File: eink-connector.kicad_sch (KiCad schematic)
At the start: 6 parts, among them J2 FFC-FPC_1X24_PIN

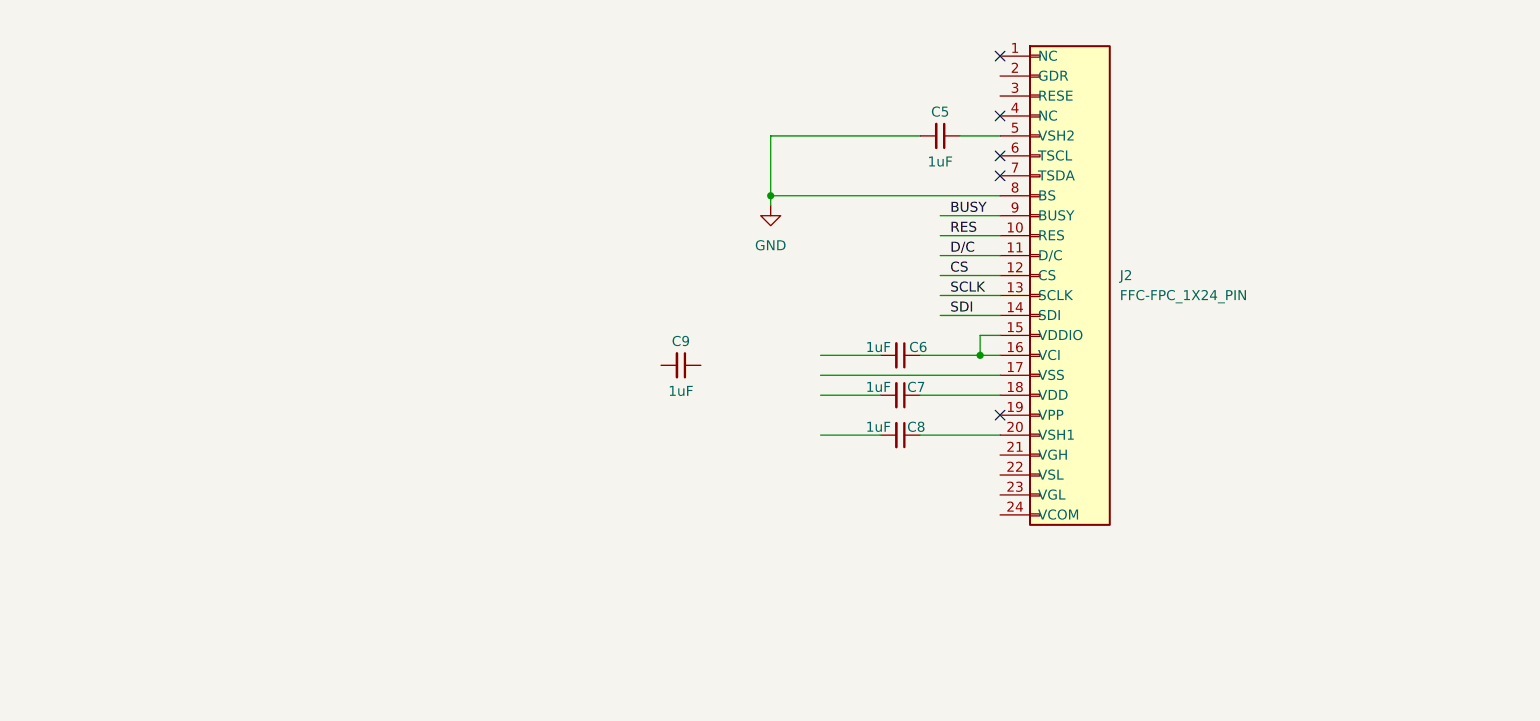
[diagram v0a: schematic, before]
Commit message: eink-> mcu connections
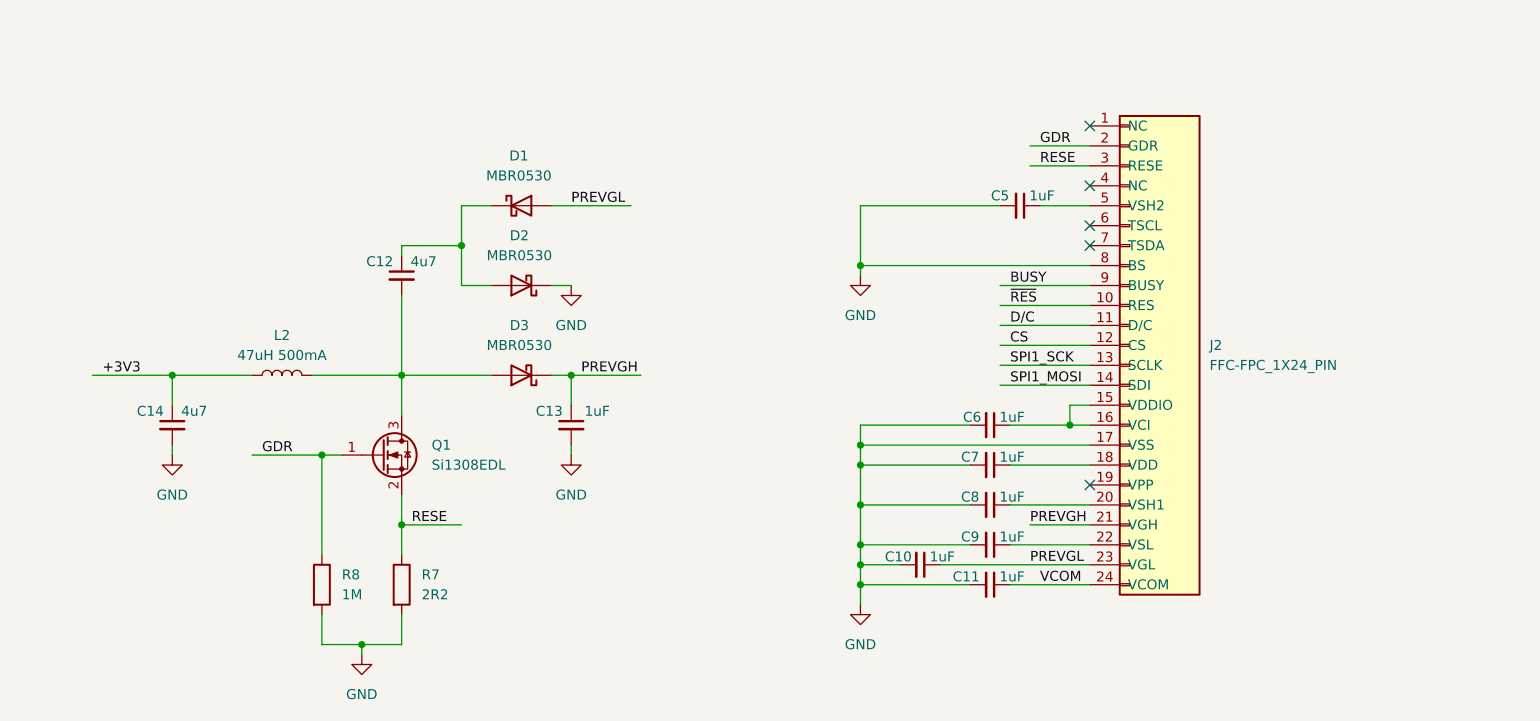
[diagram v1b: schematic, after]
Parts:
- added C10, C11, C13: 1uF, Capacitor_SMD:C_0603_1608Metric, symbol Device:C_Small
- added C12, C14: 4u7, Capacitor_SMD:C_0603_1608Metric, symbol Device:C_Small
- added D1, D2, D3: MBR0530, Diode_SMD:D_SOD-123, symbol Diode:MBR0530
- added L2: 47uH 500mA, 47uH 500mA, symbol Device:L
- added Q1: Si1308EDL, Package_TO_SOT_SMD:SOT-323_SC-70, symbol Transistor_FET:Si1308EDL
- added R7: 2R2, Resistor_SMD:R_0201_0603Metric, symbol Device:R
- added R8: 1M, Resistor_SMD:R_0201_0603Metric, symbol Device:R
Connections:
- net GND: now also C6.2, C7.2, C8.2, C9.2, J2.17 (VSS), C10.2, C11.2, C13.2, C14.2, D2.1 (K), R7.2, R8.2
- net GDR: now reaches J2.2 (GDR)
- net GDR: now also Q1.1 (G), R8.1
- net PREVGH: now reaches J2.21 (VGH)
- net PREVGH: now also C13.1, D3.1 (K)
- net at J2.22 (VSL): now also C9.1
- net PREVGL: now reaches J2.23 (VGL)
- net PREVGL: now also C10.1, D1.2 (A)
- net VCOM: now reaches J2.24 (VCOM)
- net VCOM: now also C11.1
- net RESE: now reaches J2.3 (RESE)
- net RESE: now also Q1.2 (S), R7.1
- net RES renamed ~{RES}
- net SCLK renamed SPI1_SCK
- net SDI renamed SPI1_MOSI
- new net: C12.2, D3.2 (A), L2.2, Q1.3 (D)
- new net: C12.1, D1.1 (K), D2.2 (A)
- new net +3V3: C14.1, L2.1
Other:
- moved on the sheet: C5, C6, C7, J2

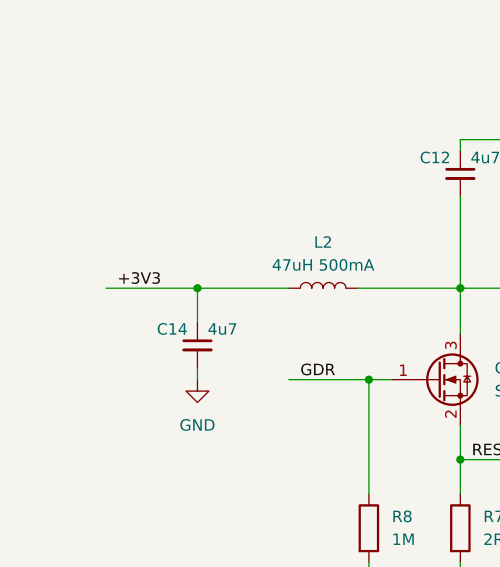
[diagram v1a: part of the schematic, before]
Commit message: added externals crystal oscillators
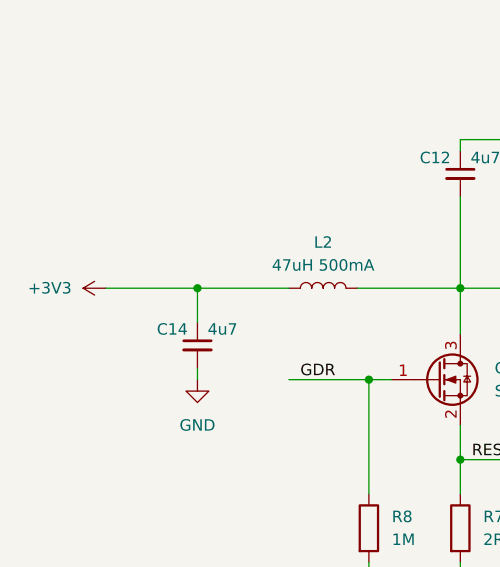
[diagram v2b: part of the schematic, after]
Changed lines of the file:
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@@
-		)
-	)
-	(label "+3V3"
-		(at 72.39 95.25 0)
-		(effects
-			(font
-				(size 1.27 1.27)
-			)
-			(justify left bottom)
 		)
 	)
@@
 					(unit 1)
 				)
+			)
+		)
+	)
+	(symbol
+		(lib_id "power:+3V3")
+		(at 71.12 95.25 90)
+		(unit 1)
+		(exclude_from_sim no)
+		(in_bom yes)
+		(on_board yes)
+		(dnp no)
+		(fields_autoplaced yes)
+		(property "Reference" "#PWR025"
+			(at 74.93 95.25 0)
+			(effects
+				(font
+					(size 1.27 1.27)
+				)
+				(hide yes)
+			)
+		)
+		(property "Value" "+3V3"
+			(at 67.31 95.2499 90)
+			(effects
+				(font
+					(size 1.27 1.27)
+				)
+				(justify left)
+			)
+		)
+		(property "Footprint" ""
+			(at 71.12 95.25 0)
+			(effects
+				(font
+					(size 1.27 1.27)
+				)
+				(hide yes)
+			)
+		)
+		(property "Datasheet" ""
+			(at 71.12 95.25 0)
+			(effects
+				(font
+					(size 1.27 1.27)
+				)
+				(hide yes)
+			)
+		)
+		(property "Description" "Power symbol creates a global label with name \"+3V3\""
+			(at 71.12 95.25 0)
+			(effects
+				(font
+					(size 1.27 1.27)
+				)
+				(hide yes)
+			)
+		)
+		(pin "1"
+		)
+		(instances
+			(project ""
+				(path "/29eb74dc-e91c-4cc5-ad9f-7f8caf36d690/d1e239c8-1e89-4f3e-9b45-1354c48c8e66"
+					(reference "#PWR025")
+					(unit 1)
+				)

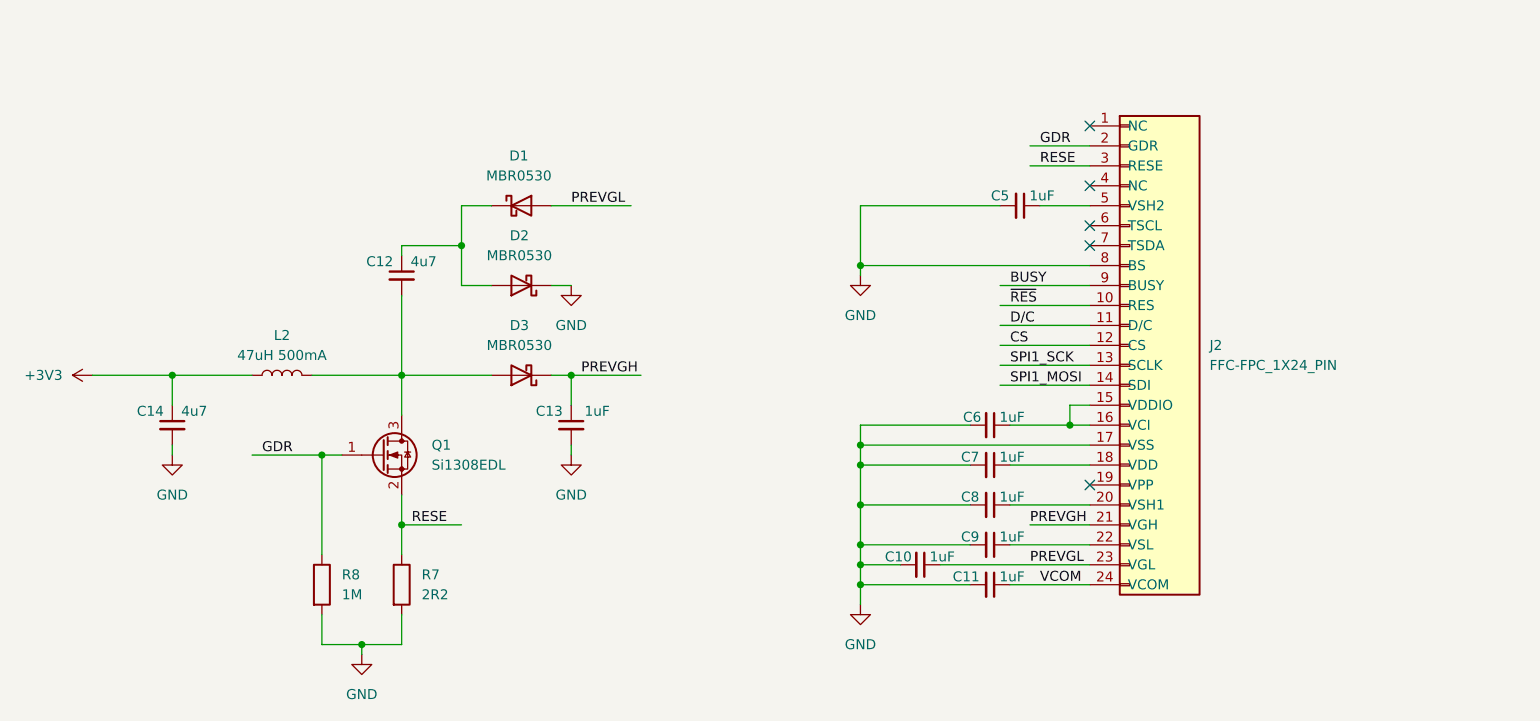
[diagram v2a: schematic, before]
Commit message: cleaned up some net labels for ERC
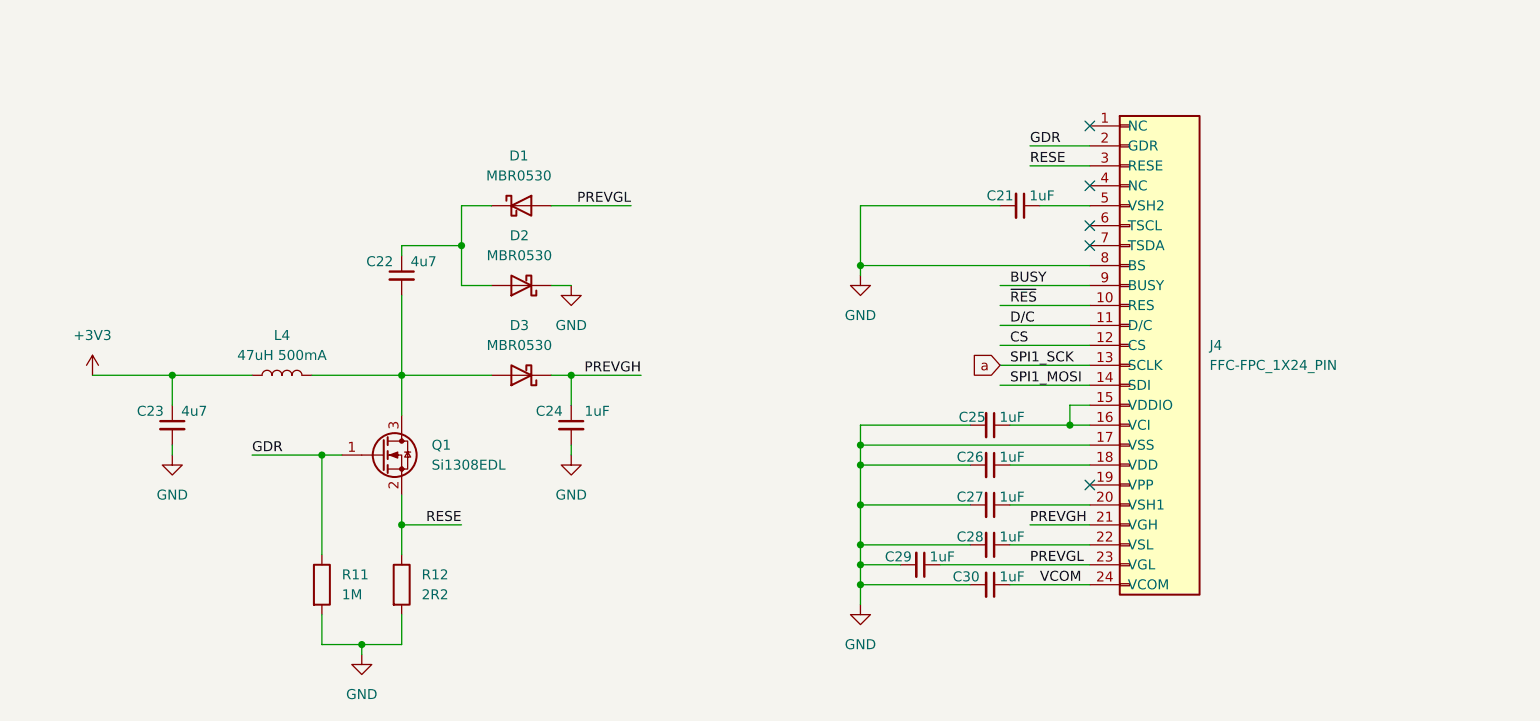
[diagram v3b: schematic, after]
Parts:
- L4: renamed from L2; footprint 47uH 500mA -> (none)
- renumbered C5 to C21, C12 to C22, C14 to C23, C13 to C24, C6 to C25, C7 to C26, C8 to C27, C9 to C28, C10 to C29, C11 to C30, J2 to J4, R8 to R11, R7 to R12
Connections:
- net SPI1_SCK renamed a
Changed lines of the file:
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@@
 	(wire
 		(pts
-			(xy 139.7 73.66) (xy 129.54 73.66)
+			(xy 129.54 73.66) (xy 139.7 73.66)
 		)
 		(stroke
@@
 	(wire
 		(pts
+			(xy 91.44 105.41) (xy 100.33 105.41)
+		)
+		(stroke
+			(width 0)
+			(type default)
+		)
+	)
+	(wire
+		(pts
 			(xy 118.11 73.66) (xy 121.92 73.66)
 		)
@@
 		(pts
 			(xy 168.91 73.66) (xy 186.69 73.66)
-		)
-		(stroke
-			(width 0)
-			(type default)
-		)
-	)
-	(wire
-		(pts
-			(xy 91.44 105.41) (xy 100.33 105.41)
 		)
 		(stroke
@@
 	)
 	(label "RESE"
-		(at 191.77 68.58 0)
+		(at 190.5 68.58 0)
 		(effects
 			(font
@@
 	)
 	(label "PREVGL"
-		(at 132.08 73.66 0)
+		(at 139.7 73.66 180)
 		(effects
 			(font
 				(size 1.27 1.27)
 			)
-			(justify left bottom)
+			(justify right bottom)
 		)
 	)
@@
 	)
 	(label "PREVGH"
-		(at 133.35 95.25 0)
+		(at 140.97 95.25 180)
 		(effects
 			(font
 				(size 1.27 1.27)
 			)
-			(justify left bottom)
+			(justify right bottom)
 		)
 	)
@@
 	)
 	(label "GDR"
-		(at 191.77 66.04 0)
+		(at 190.5 66.04 0)
 		(effects
 			(font
@@
 	)
 	(label "RESE"
-		(at 111.76 114.3 0)
+		(at 118.11 114.3 180)
 		(effects
 			(font
 				(size 1.27 1.27)
 			)
-			(justify left bottom)
+			(justify right bottom)
 		)
 	)
@@
 	)
 	(label "GDR"
-		(at 92.71 105.41 0)
+		(at 91.44 105.41 0)
 		(effects
 			(font
@@
 		)
 	)
+	(global_label "a"
+		(shape input)
+		(at 186.69 93.98 180)
+		(fields_autoplaced yes)
+		(effects
+			(font
+				(size 1.27 1.27)
+			)
+			(justify right)
+		)
+		(property "Intersheetrefs" "${INTERSHEET_REFS}"
+			(at 182.5558 93.98 0)
+			(effects
+				(font
+					(size 1.27 1.27)
+				)
+				(justify right)
+				(hide yes)
+			)
+		)
+	)
 	(symbol
 		(lib_id "Diode:MBR0530")
@@
 		(on_board yes)
 		(dnp no)
-		(property "Reference" "#PWR013"
+		(property "Reference" "#PWR039"
 			(at 168.91 130.81 0)
 			(effects
@@
 			(project "2tonewatch"
 				(path "/29eb74dc-e91c-4cc5-ad9f-7f8caf36d690/d1e239c8-1e89-4f3e-9b45-1354c48c8e66"
-					(reference "#PWR013")
+					(reference "#PWR039")
 					(unit 1)
 				)
@@
 		(on_board yes)
 		(dnp no)
-		(property "Reference" "C12"
+		(property "Reference" "C22"
 			(at 107.696 80.772 0)
 			(effects
@@
 			(project "2tonewatch"
 				(path "/29eb74dc-e91c-4cc5-ad9f-7f8caf36d690/d1e239c8-1e89-4f3e-9b45-1354c48c8e66"
-					(reference "C12")
+					(reference "C22")
 					(unit 1)
 				)
@@
 	(symbol
 		(lib_id "power:+3V3")
-		(at 71.12 95.25 90)
+		(at 71.12 95.25 0)
 		(unit 1)
 		(exclude_from_sim no)
@@
 		(dnp no)
 		(fields_autoplaced yes)
-		(property "Reference" "#PWR025"
-			(at 74.93 95.25 0)
+		(property "Reference" "#PWR036"
+			(at 71.12 99.06 0)
 			(effects
 				(font
@@
 		)
 		(property "Value" "+3V3"
-			(at 67.31 95.2499 90)
-			(effects
-				(font
-					(size 1.27 1.27)
-				)
-				(justify left)
+			(at 71.12 90.17 0)
+			(effects
+				(font
+					(size 1.27 1.27)
+				)
 			)
 		)
@@
 			(project ""
 				(path "/29eb74dc-e91c-4cc5-ad9f-7f8caf36d690/d1e239c8-1e89-4f3e-9b45-1354c48c8e66"
-					(reference "#PWR025")
+					(reference "#PWR036")
 					(unit 1)
 				)
@@
 		(on_board yes)
 		(dnp no)
-		(property "Reference" "C11"
+		(property "Reference" "C30"
 			(at 182.372 120.904 90)
 			(effects
@@
 			(project "2tonewatch"
 				(path "/29eb74dc-e91c-4cc5-ad9f-7f8caf36d690/d1e239c8-1e89-4f3e-9b45-1354c48c8e66"
-					(reference "C11")
+					(reference "C30")
 					(unit 1)
 				)
@@
 		(dnp no)
 		(fields_autoplaced yes)
-		(property "Reference" "L2"
+		(property "Reference" "L4"
 			(at 95.25 90.17 90)
 			(effects
@@
 			)
 		)
-		(property "Footprint" "47uH 500mA"
+		(property "Footprint" ""
 			(at 95.25 95.25 0)
 			(effects
@@
 			(project ""
 				(path "/29eb74dc-e91c-4cc5-ad9f-7f8caf36d690/d1e239c8-1e89-4f3e-9b45-1354c48c8e66"
-					(reference "L2")
+					(reference "L4")
 					(unit 1)
 				)
@@
 		(on_board yes)
 		(dnp no)
-		(property "Reference" "#PWR015"
+		(property "Reference" "#PWR038"
 			(at 132.08 111.76 0)
 			(effects
@@
 			(project "2tonewatch"
 				(path "/29eb74dc-e91c-4cc5-ad9f-7f8caf36d690/d1e239c8-1e89-4f3e-9b45-1354c48c8e66"
-					(reference "#PWR015")
+					(reference "#PWR038")
 					(unit 1)
 				)
@@
 		(on_board yes)
 		(dnp no)
-		(property "Reference" "C9"
+		(property "Reference" "C28"
 			(at 182.88 115.824 90)
 			(effects
@@
 			(project "2tonewatch"
 				(path "/29eb74dc-e91c-4cc5-ad9f-7f8caf36d690/d1e239c8-1e89-4f3e-9b45-1354c48c8e66"
-					(reference "C9")
+					(reference "C28")
 					(unit 1)
 				)
@@
 		(on_board yes)
 		(dnp no)
-		(property "Reference" "C7"
+		(property "Reference" "C26"
 			(at 182.88 105.664 90)
 			(effects
@@
 			(project "2tonewatch"
 				(path "/29eb74dc-e91c-4cc5-ad9f-7f8caf36d690/d1e239c8-1e89-4f3e-9b45-1354c48c8e66"
-					(reference "C7")
+					(reference "C26")
 					(unit 1)
 				)
@@
 		(on_board yes)
 		(dnp no)
-		(property "Reference" "C5"
+		(property "Reference" "C21"
 			(at 186.69 72.39 90)
 			(effects
@@
 			(project ""
 				(path "/29eb74dc-e91c-4cc5-ad9f-7f8caf36d690/d1e239c8-1e89-4f3e-9b45-1354c48c8e66"
-					(reference "C5")
+					(reference "C21")
 					(unit 1)
 				)
@@
 		(on_board yes)
 		(dnp no)
-		(property "Reference" "C14"
+		(property "Reference" "C23"
 			(at 78.486 99.822 0)
 			(effects
@@
 			(project "2tonewatch"
 				(path "/29eb74dc-e91c-4cc5-ad9f-7f8caf36d690/d1e239c8-1e89-4f3e-9b45-1354c48c8e66"
-					(reference "C14")
+					(reference "C23")
 					(unit 1)
 				)
@@
 		(on_board yes)
 		(dnp no)
-		(property "Reference" "#PWR01"
+		(property "Reference" "#PWR034"
 			(at 168.91 88.9 0)
 			(effects
@@
 			(project ""
 				(path "/29eb74dc-e91c-4cc5-ad9f-7f8caf36d690/d1e239c8-1e89-4f3e-9b45-1354c48c8e66"
-					(reference "#PWR01")
+					(reference "#PWR034")
 					(unit 1)
 				)
@@
 		(on_board yes)
 		(dnp no)
-		(property "Reference" "C10"
+		(property "Reference" "C29"
 			(at 173.736 118.364 90)
 			(effects
@@
 			(project "2tonewatch"
 				(path "/29eb74dc-e91c-4cc5-ad9f-7f8caf36d690/d1e239c8-1e89-4f3e-9b45-1354c48c8e66"
-					(reference "C10")
+					(reference "C29")
 					(unit 1)
 				)
@@
 		(on_board yes)
 		(dnp no)
-		(property "Reference" "C6"
+		(property "Reference" "C25"
 			(at 183.134 100.584 90)
 			(effects
@@
 			(project "2tonewatch"
 				(path "/29eb74dc-e91c-4cc5-ad9f-7f8caf36d690/d1e239c8-1e89-4f3e-9b45-1354c48c8e66"
-					(reference "C6")
+					(reference "C25")
 					(unit 1)
 				)
@@
 		(on_board yes)
 		(dnp no)
-		(property "Reference" "#PWR014"
+		(property "Reference" "#PWR035"
 			(at 132.08 90.17 0)
 			(effects
@@
 			(project "2tonewatch"
 				(path "/29eb74dc-e91c-4cc5-ad9f-7f8caf36d690/d1e239c8-1e89-4f3e-9b45-1354c48c8e66"
-					(reference "#PWR014")
+					(reference "#PWR035")
 					(unit 1)
 				)
@@
 		(dnp no)
 		(fields_autoplaced yes)
-		(property "Reference" "R7"
+		(property "Reference" "R12"
 			(at 113.03 120.6499 0)
 			(effects
@@
 			(project ""
 				(path "/29eb74dc-e91c-4cc5-ad9f-7f8caf36d690/d1e239c8-1e89-4f3e-9b45-1354c48c8e66"
-					(reference "R7")
+					(reference "R12")
 					(unit 1)
 				)
@@
 		(on_board yes)
 		(dnp no)
-		(property "Reference" "J2"
+		(property "Reference" "J4"
 			(at 213.36 91.4399 0)
 			(effects
@@
 			(project "2tonewatch"
 				(path "/29eb74dc-e91c-4cc5-ad9f-7f8caf36d690/d1e239c8-1e89-4f3e-9b45-1354c48c8e66"
-					(reference "J2")
+					(reference "J4")
 					(unit 1)
 				)
@@
 		(on_board yes)
 		(dnp no)
-		(property "Reference" "#PWR017"
+		(property "Reference" "#PWR037"
 			(at 81.28 111.76 0)
 			(effects
@@
 			(project "2tonewatch"
 				(path "/29eb74dc-e91c-4cc5-ad9f-7f8caf36d690/d1e239c8-1e89-4f3e-9b45-1354c48c8e66"
-					(reference "#PWR017")
+					(reference "#PWR037")
 					(unit 1)
 				)
@@
 		(on_board yes)
 		(dnp no)
-		(property "Reference" "C8"
+		(property "Reference" "C27"
 			(at 182.88 110.744 90)
 			(effects
@@
 			(project "2tonewatch"
 				(path "/29eb74dc-e91c-4cc5-ad9f-7f8caf36d690/d1e239c8-1e89-4f3e-9b45-1354c48c8e66"
-					(reference "C8")
+					(reference "C27")
 					(unit 1)
 				)
@@
 		(on_board yes)
 		(dnp no)
-		(property "Reference" "C13"
+		(property "Reference" "C24"
 			(at 129.286 99.822 0)
 			(effects
@@
 			(project "2tonewatch"
 				(path "/29eb74dc-e91c-4cc5-ad9f-7f8caf36d690/d1e239c8-1e89-4f3e-9b45-1354c48c8e66"
-					(reference "C13")
+					(reference "C24")
 					(unit 1)
 				)
@@
 		(dnp no)
 		(fields_autoplaced yes)
-		(property "Reference" "R8"
+		(property "Reference" "R11"
 			(at 102.87 120.6499 0)
 			(effects
@@
 			(project "2tonewatch"
 				(path "/29eb74dc-e91c-4cc5-ad9f-7f8caf36d690/d1e239c8-1e89-4f3e-9b45-1354c48c8e66"
-					(reference "R8")
+					(reference "R11")
 					(unit 1)
 				)
@@
 		(on_board yes)
 		(dnp no)
-		(property "Reference" "#PWR016"
+		(property "Reference" "#PWR040"
 			(at 105.41 137.16 0)
 			(effects
@@
 			(project "2tonewatch"
 				(path "/29eb74dc-e91c-4cc5-ad9f-7f8caf36d690/d1e239c8-1e89-4f3e-9b45-1354c48c8e66"
-					(reference "#PWR016")
-					(unit 1)
-				)
+					(reference "#PWR040")
+					(unit 1)
+				)
